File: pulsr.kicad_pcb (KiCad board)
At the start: 2 copper layers, 90.9 x 94.1 mm, 243 parts, among them J1 JST_PH, J2 0.1" header, Q1 FDN339AN

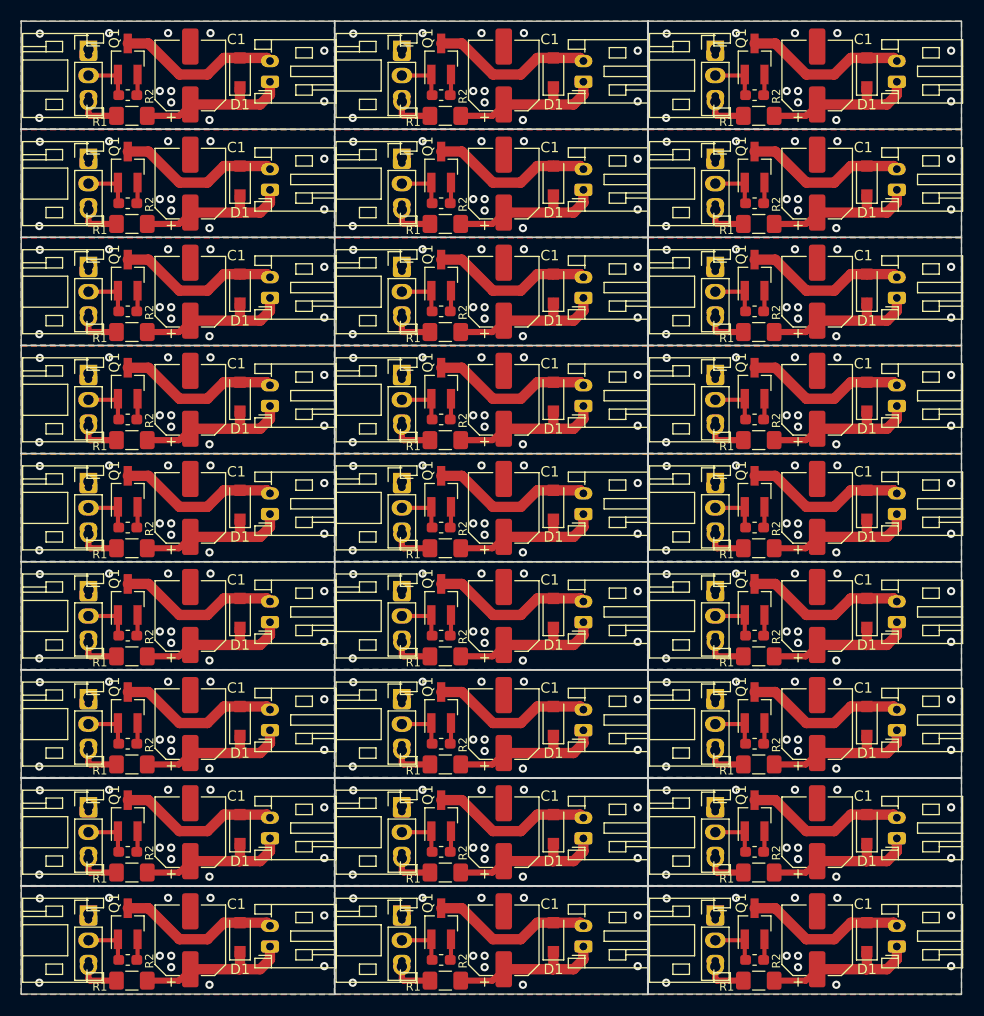
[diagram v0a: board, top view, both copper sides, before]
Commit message: fixed overwritten files
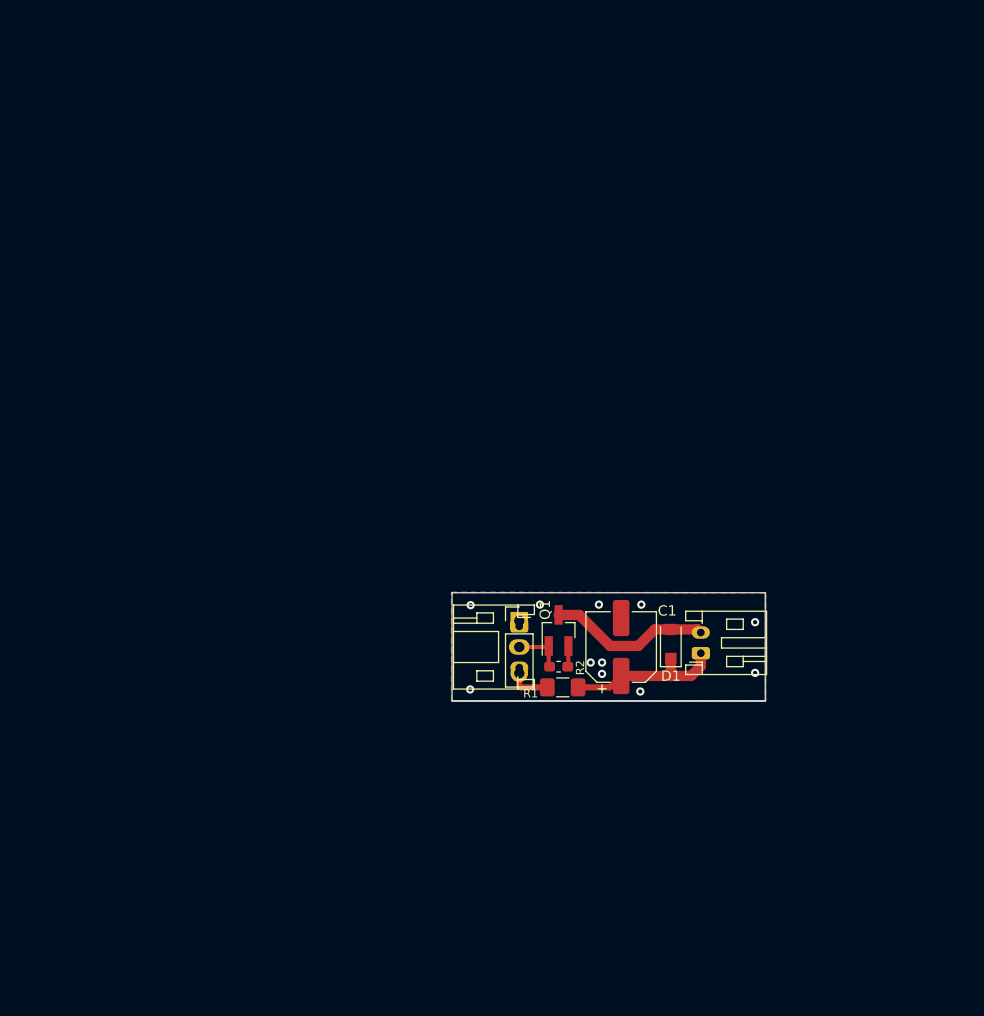
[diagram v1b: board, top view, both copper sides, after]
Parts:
- removed the C1 at (166.9, 129.7)
- removed the C1 at (166.9, 98.3)
- removed the C1 at (136.6, 98.3)
- removed the C1 at (106.3, 98.3)
- removed the C1 at (166.9, 87.9)
- removed the C1 at (136.6, 87.9)
- removed the C1 at (106.3, 87.9)
- removed the C1 at (166.9, 77.5)
- removed the C1 at (136.6, 77.5)
- removed the C1 at (106.3, 77.5)
- removed the C1 at (166.9, 67.0)
- removed the C1 at (136.6, 129.7)
- removed the C1 at (136.6, 67.0)
- removed the C1 at (106.3, 67.0)
- removed the C1 at (166.9, 56.5)
- removed the C1 at (136.6, 56.5)
- removed the C1 at (106.3, 56.5)
- removed the C1 at (166.9, 46.1)
- removed the C1 at (136.6, 46.1)
- removed the C1 at (106.3, 129.7)
- removed the C1 at (166.9, 119.2)
- removed the C1 at (136.6, 119.2)
- removed the C1 at (106.3, 119.2)
- removed the C1 at (166.9, 108.8)
- removed the C1 at (136.6, 108.8)
- removed the C1 at (106.3, 108.8)
- removed the D1 at (171.7, 129.4)
- removed the D1 at (171.7, 98.0)
- removed the D1 at (141.4, 98.0)
- removed the D1 at (111.1, 98.0)
- removed the D1 at (171.7, 87.6)
- removed the D1 at (141.4, 87.6)
- removed the D1 at (111.1, 87.6)
- removed the D1 at (171.7, 77.2)
- removed the D1 at (141.4, 77.2)
- removed the D1 at (111.1, 77.2)
- removed the D1 at (171.7, 66.7)
- removed the D1 at (141.4, 129.4)
- removed the D1 at (141.4, 66.7)
- removed the D1 at (111.1, 66.7)
- removed the D1 at (171.7, 56.2)
- removed the D1 at (141.4, 56.2)
- removed the D1 at (111.1, 56.2)
- removed the D1 at (171.7, 45.8)
- removed the D1 at (141.4, 45.8)
- removed the D1 at (111.1, 129.4)
- removed the D1 at (171.7, 119.0)
- removed the D1 at (141.4, 119.0)
- removed the D1 at (111.1, 119.0)
- removed the D1 at (171.7, 108.5)
- removed the D1 at (141.4, 108.5)
- removed the D1 at (111.1, 108.5)
- removed the G*** at (165.6, 130.2)
- removed the G*** at (165.6, 98.8)
- removed the G*** at (135.3, 98.8)
- removed the G*** at (105.0, 98.8)
- removed the G*** at (165.6, 88.4)
- removed the G*** at (135.3, 88.4)
- removed the G*** at (105.0, 88.4)
- removed the G*** at (165.6, 78.0)
- removed the G*** at (135.3, 78.0)
- removed the G*** at (105.0, 78.0)
- removed the G*** at (165.6, 67.5)
- removed the G*** at (135.3, 130.2)
- removed the G*** at (135.3, 67.5)
- removed the G*** at (105.0, 67.5)
- removed the G*** at (165.6, 57.0)
- removed the G*** at (135.3, 57.0)
- removed the G*** at (105.0, 57.0)
- removed the G*** at (165.6, 46.6)
- removed the G*** at (135.3, 46.6)
- removed the G*** at (105.0, 130.2)
- removed the G*** at (165.6, 119.8)
- removed the G*** at (135.3, 119.8)
- removed the G*** at (105.0, 119.8)
- removed the G*** at (165.6, 109.3)
- removed the G*** at (135.3, 109.3)
- removed the G*** at (105.0, 109.3)
- removed the J1 at (157.1, 127.7)
- removed the J1 at (157.1, 96.3)
- removed the J1 at (126.8, 96.3)
- removed the J1 at (96.5, 96.3)
- removed the J1 at (157.1, 85.9)
- removed the J1 at (126.8, 85.9)
- removed the J1 at (96.5, 85.9)
- removed the J1 at (157.1, 75.5)
- removed the J1 at (126.8, 75.5)
- removed the J1 at (96.5, 75.5)
- removed the J1 at (157.1, 65.0)
- removed the J1 at (126.8, 127.7)
- removed the J1 at (126.8, 65.0)
- removed the J1 at (96.5, 65.0)
- removed the J1 at (157.1, 54.5)
- removed the J1 at (126.8, 54.5)
- removed the J1 at (96.5, 54.5)
- removed the J1 at (157.1, 44.1)
- removed the J1 at (126.8, 44.1)
- removed the J1 at (96.5, 127.7)
- removed the J1 at (157.1, 117.2)
- removed the J1 at (126.8, 117.2)
- removed the J1 at (96.5, 117.2)
- removed the J1 at (157.1, 106.8)
- removed the J1 at (126.8, 106.8)
- removed the J1 at (96.5, 106.8)
- removed the J2 at (157.1, 127.2)
- removed the J2 at (157.1, 95.8)
- removed the J2 at (126.8, 95.8)
- removed the J2 at (96.5, 95.8)
- removed the J2 at (157.1, 85.4)
- removed the J2 at (126.8, 85.4)
- removed the J2 at (96.5, 85.4)
- removed the J2 at (157.1, 74.9)
- removed the J2 at (126.8, 74.9)
- removed the J2 at (96.5, 74.9)
- removed the J2 at (157.1, 64.5)
- removed the J2 at (126.8, 127.2)
- removed the J2 at (126.8, 64.5)
- removed the J2 at (96.5, 64.5)
- removed the J2 at (157.1, 54.0)
- removed the J2 at (126.8, 54.0)
- removed the J2 at (96.5, 54.0)
- removed the J2 at (157.1, 43.6)
- removed the J2 at (126.8, 43.6)
- removed the J2 at (96.5, 127.2)
- removed the J2 at (157.1, 116.7)
- removed the J2 at (126.8, 116.7)
- removed the J2 at (96.5, 116.7)
- removed the J2 at (157.1, 106.3)
- removed the J2 at (126.8, 106.3)
- removed the J2 at (96.5, 106.3)
- removed the L1 at (174.6, 130.3)
- removed the L1 at (174.6, 99.0)
- removed the L1 at (144.3, 99.0)
- removed the L1 at (114.0, 99.0)
- removed the L1 at (174.6, 88.5)
- removed the L1 at (144.3, 88.5)
- removed the L1 at (114.0, 88.5)
- removed the L1 at (174.6, 78.0)
- removed the L1 at (144.3, 78.0)
- removed the L1 at (114.0, 78.0)
- removed the L1 at (174.6, 67.6)
- removed the L1 at (144.3, 130.3)
- removed the L1 at (144.3, 67.6)
- removed the L1 at (114.0, 67.6)
- removed the L1 at (174.6, 57.1)
- removed the L1 at (144.3, 57.1)
- removed the L1 at (114.0, 57.1)
- removed the L1 at (174.6, 46.7)
- removed the L1 at (144.3, 46.7)
- removed the L1 at (114.0, 130.3)
- removed the L1 at (174.6, 119.8)
- removed the L1 at (144.3, 119.8)
- removed the L1 at (114.0, 119.8)
- removed the L1 at (174.6, 109.4)
- removed the L1 at (144.3, 109.4)
- removed the L1 at (114.0, 109.4)
- removed the Q1 at (160.8, 128.1)
- removed the Q1 at (160.8, 96.8)
- removed the Q1 at (130.6, 96.8)
- removed the Q1 at (100.2, 96.8)
- removed the Q1 at (160.8, 86.3)
- removed the Q1 at (130.6, 86.3)
- removed the Q1 at (100.2, 86.3)
- removed the Q1 at (160.8, 75.8)
- removed the Q1 at (130.6, 75.8)
- removed the Q1 at (100.2, 75.8)
- removed the Q1 at (160.8, 65.4)
- removed the Q1 at (130.6, 128.1)
- removed the Q1 at (130.6, 65.4)
- removed the Q1 at (100.2, 65.4)
- removed the Q1 at (160.8, 55.0)
- removed the Q1 at (130.6, 55.0)
- removed the Q1 at (100.2, 55.0)
- removed the Q1 at (160.8, 44.5)
- removed the Q1 at (130.6, 44.5)
- removed the Q1 at (100.2, 128.1)
- removed the Q1 at (160.8, 117.7)
- removed the Q1 at (130.6, 117.7)
- removed the Q1 at (100.2, 117.7)
- removed the Q1 at (160.8, 107.2)
- removed the Q1 at (130.6, 107.2)
- removed the Q1 at (100.2, 107.2)
- removed the R1 at (161.2, 133.6)
- removed the R1 at (161.2, 102.2)
- removed the R1 at (130.9, 102.2)
- removed the R1 at (100.7, 102.2)
- removed the R1 at (161.2, 91.8)
- removed the R1 at (130.9, 91.8)
- removed the R1 at (100.7, 91.8)
- removed the R1 at (161.2, 81.3)
- removed the R1 at (130.9, 81.3)
- removed the R1 at (100.7, 81.3)
- removed the R1 at (161.2, 70.9)
- removed the R1 at (130.9, 133.6)
- removed the R1 at (130.9, 70.9)
- removed the R1 at (100.7, 70.9)
- removed the R1 at (161.2, 60.5)
- removed the R1 at (130.9, 60.5)
- removed the R1 at (100.7, 60.5)
- removed the R1 at (161.2, 50.0)
- removed the R1 at (130.9, 50.0)
- removed the R1 at (100.7, 133.6)
- removed the R1 at (161.2, 123.2)
- removed the R1 at (130.9, 123.2)
- removed the R1 at (100.7, 123.2)
- removed the R1 at (161.2, 112.7)
- removed the R1 at (130.9, 112.7)
- removed the R1 at (100.7, 112.7)
- removed the R2 at (160.8, 131.6)
- removed the R2 at (160.8, 100.2)
- removed the R2 at (130.6, 100.2)
- removed the R2 at (100.2, 100.2)
- removed the R2 at (160.8, 89.8)
- removed the R2 at (130.6, 89.8)
- removed the R2 at (100.2, 89.8)
- removed the R2 at (160.8, 79.3)
- removed the R2 at (130.6, 79.3)
- removed the R2 at (100.2, 79.3)
- removed the R2 at (160.8, 68.9)
- removed the R2 at (130.6, 131.6)
- removed the R2 at (130.6, 68.9)
- removed the R2 at (100.2, 68.9)
- removed the R2 at (160.8, 58.5)
- removed the R2 at (130.6, 58.5)
- removed the R2 at (100.2, 58.5)
- removed the R2 at (160.8, 48.0)
- removed the R2 at (130.6, 48.0)
- removed the R2 at (100.2, 131.6)
- removed the R2 at (160.8, 121.2)
- removed the R2 at (130.6, 121.2)
- removed the R2 at (100.2, 121.2)
- removed the R2 at (160.8, 110.7)
- removed the R2 at (130.6, 110.7)
- removed the R2 at (100.2, 110.7)
- moved D1 69.2 mm to (152.8, 101.0)
- moved L1 69.2 mm to (155.7, 102.0)
- moved Q1 69.2 mm to (141.9, 99.8)
- moved R1 69.2 mm to (142.3, 105.2)
- moved R2 69.2 mm to (141.9, 103.2)
- moved C1 69.2 mm to (147.9, 101.3)
- moved G*** 69.2 mm to (146.7, 101.8)
- moved J1 69.2 mm to (138.1, 99.3)
- moved J2 69.2 mm to (138.1, 98.8)
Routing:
- net Net-(D1-Pad2): track 426.1 -> 15.8 mm
- net Net-(C1-Pad1): track 423.4 -> 15.7 mm
- net /FIRE!: track 132.9 -> 4.92 mm
- net +5V: track 107.5 -> 3.98 mm
- net GND: track 54.8 -> 2.03 mm, vias 297 -> 11
- removed copper zone on B.Cu, net (none)
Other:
- board size 90.9 x 94.1 mm -> 30.3 x 10.5 mm

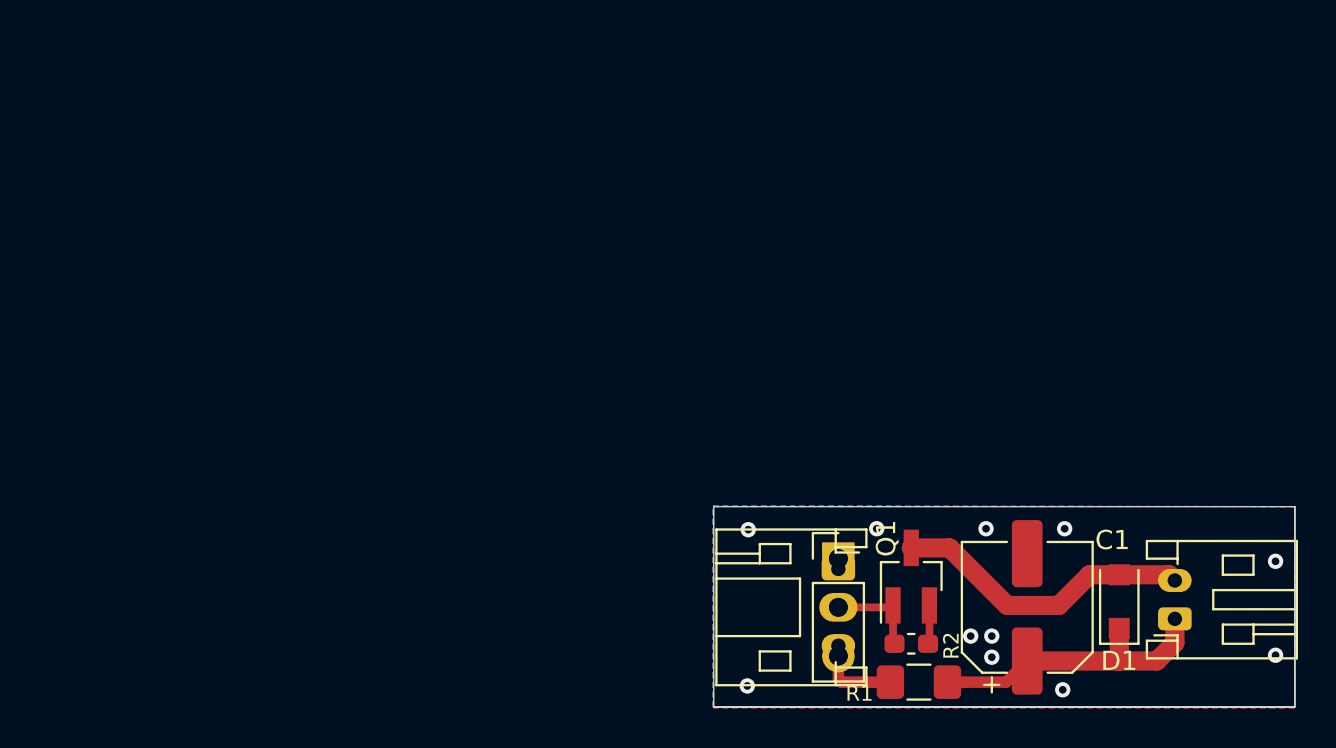
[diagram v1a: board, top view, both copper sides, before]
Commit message: Modified design to fit 47mF super-cap
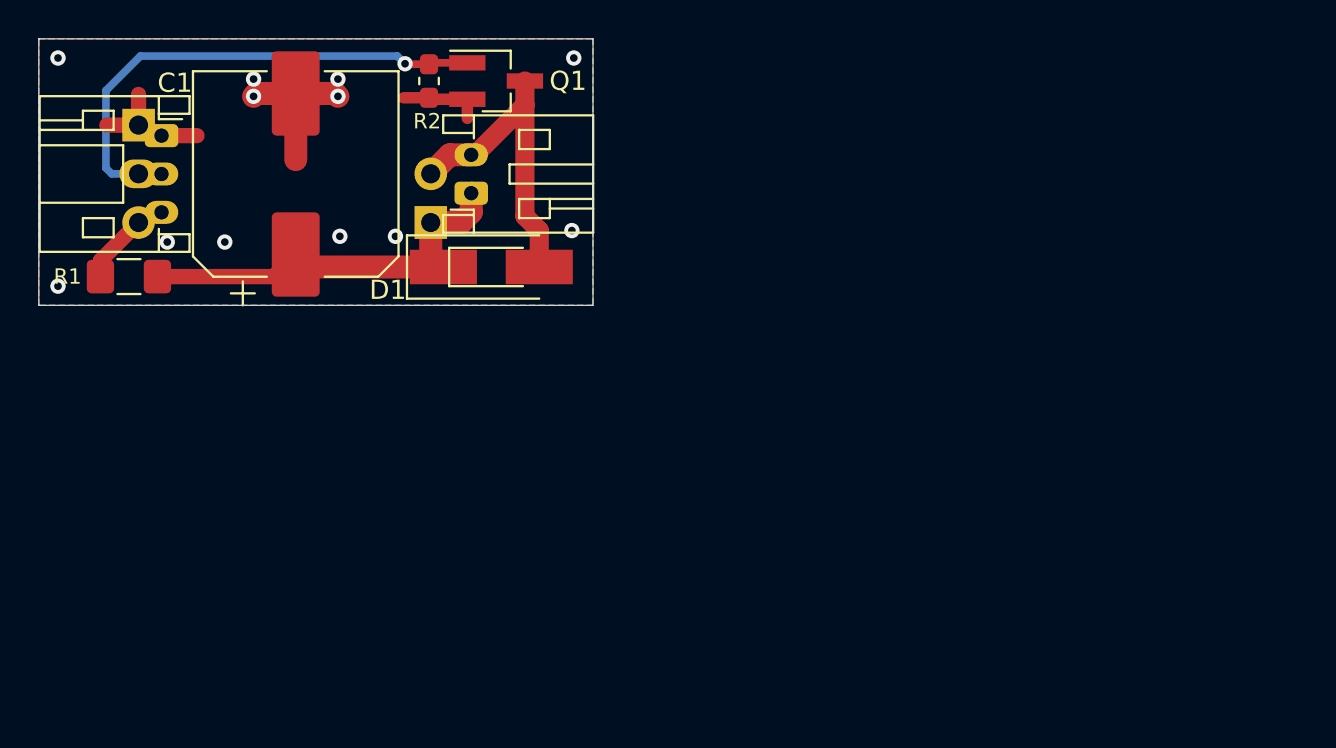
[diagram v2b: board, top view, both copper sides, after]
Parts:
- added D1: 1N4007L, Diode_SMD:D_SMA_Handsoldering, F.Cu at (120.0, 83.6)
- added J2: 0.1" header, Connector_PinHeader_2.54mm:PinHeader_1x02_P2.54mm_Vertical, F.Cu at (116.8, 81.3)
- C1: value 220uF -> FC0H473ZFTBR24; footprint Capacitor_SMD:CP_Elec_6.3x5.4 -> Capacitor_SMD:CP_Elec_10x10.5
- moved R1 46.3 mm to (101.1, 84.1)
- moved C1 44.3 mm to (109.8, 78.8)
- moved G*** 43.5 mm to (109.6, 79.1)
- moved J2 42.9 mm to (101.6, 76.2)
- moved L1 42.9 mm to (119.0, 79.8)
- moved J1 41.9 mm to (102.8, 76.8)
- moved R2 38.7 mm to (116.8, 73.9), turned to 90 degrees
- moved D1 37.1 mm to (120.0, 83.6), turned to 0 degrees
- moved Q1 33.7 mm to (120.2, 73.9), turned to 0 degrees
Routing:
- net /FIRE!: track 4.92 -> 26.9 mm, vias 0 -> 1
- net GND: track 2.03 -> 20.0 mm, vias 11 -> 12
- net Net-(C1-Pad1): track 15.7 -> 22.7 mm
- net Net-(D1-Pad2): track 15.8 -> 17.3 mm
- net +5V: track 3.98 -> 4.96 mm
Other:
- board size 30.3 x 10.5 mm -> 28.9 x 13.9 mm
- board text added: "5V"
- board text added: "FIRE!"
- board text added: "GND"
- board text added: "Pulsr"
- board text added: "v1.1.0"
- board text removed: "GND FIRE! 5V"
- board text removed: "v1.0.1"
